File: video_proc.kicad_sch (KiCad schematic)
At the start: 0 parts

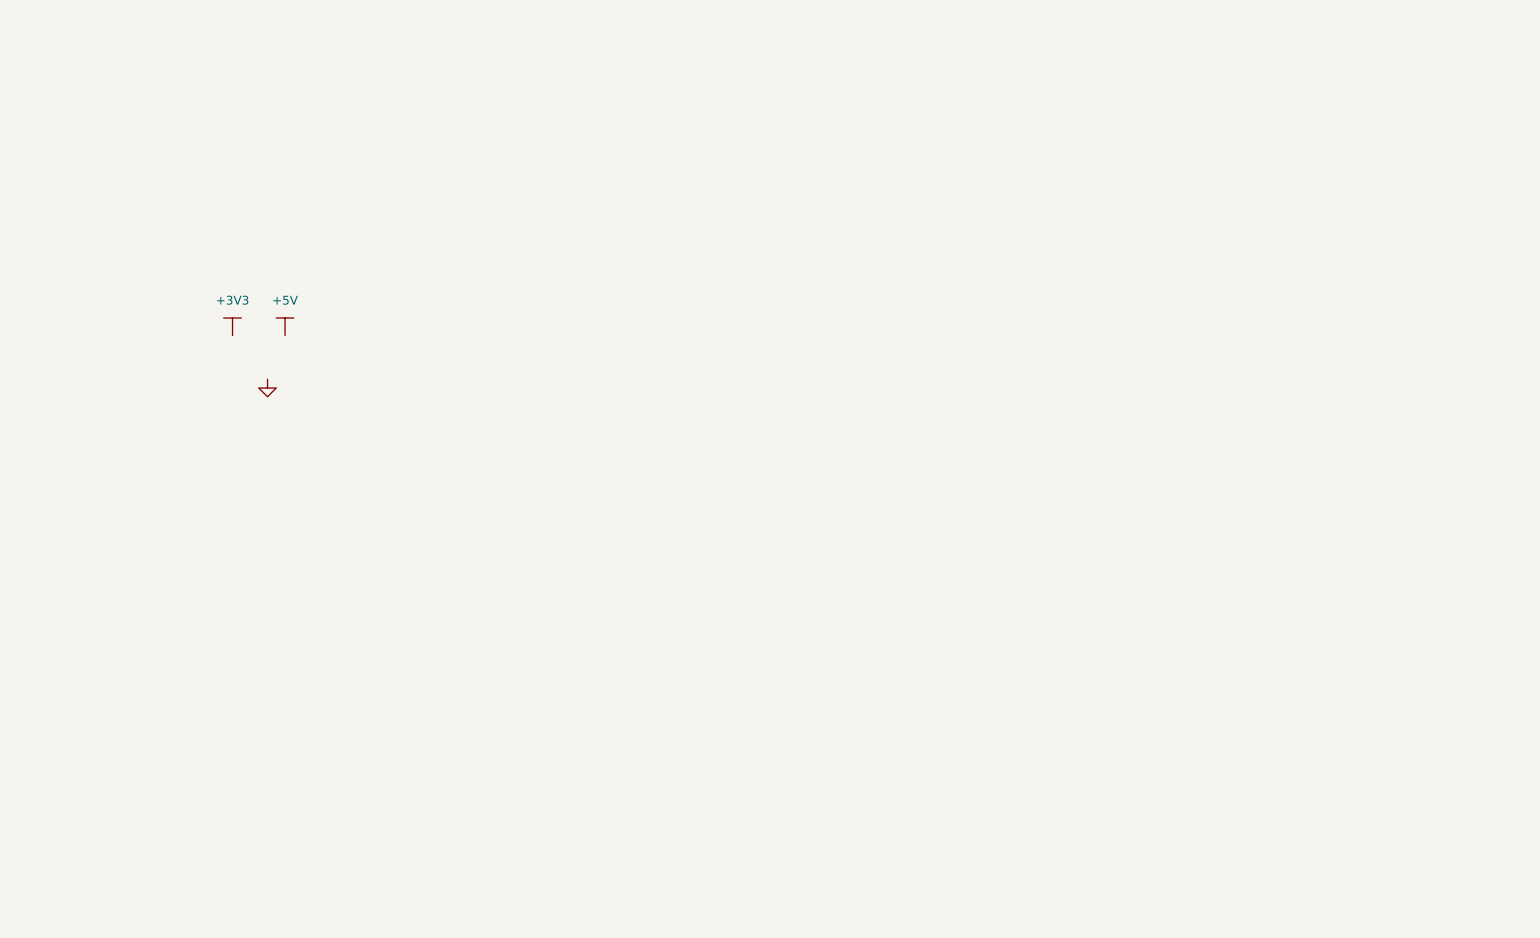
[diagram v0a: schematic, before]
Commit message: changed hierarchy, added symbols
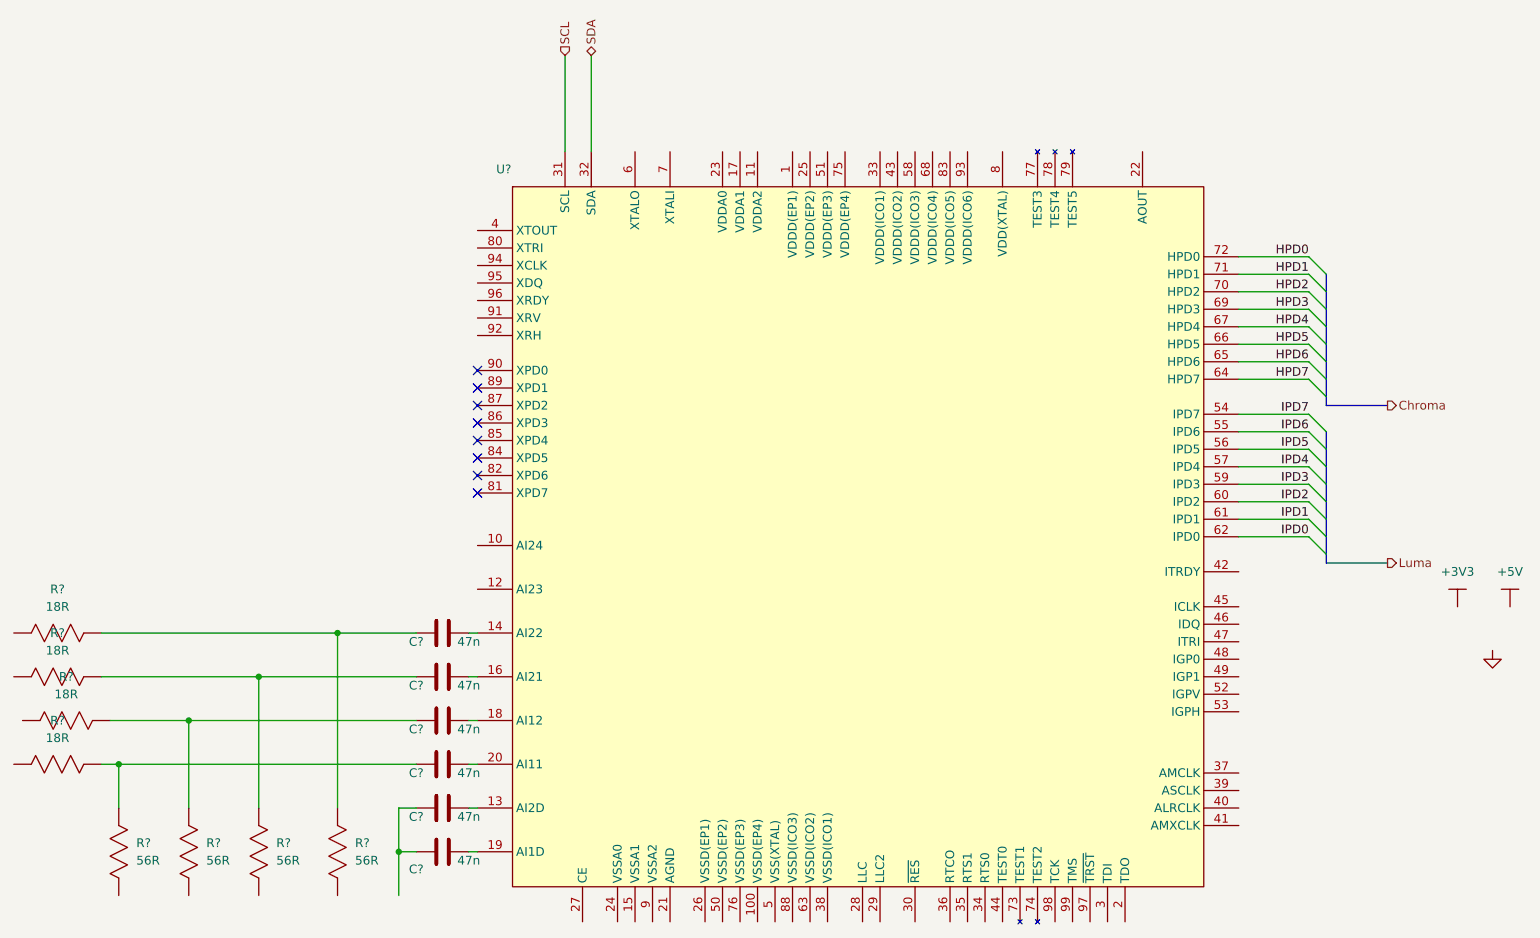
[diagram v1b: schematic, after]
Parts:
- added C? (x6): 47n, symbol tbc:GCJ188R71E473KA01D
- added R? (x4): 18R, symbol tbc:RC0603FR-0718RL
- added R? (x4): 56R, symbol tbc:RC0603FR-0756RL
- added U?: ~, symbol tbc:SAA7114H
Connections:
- new net: C?.1, R?.2, R?.2 (x4)
- new net: C?.2, U?.18 (AI12)
- new net: C?.2, U?.13 (AI2D)
- new net: C?.2, U?.14 (AI22)
- new net: C?.2, U?.16 (AI21)
- new net: C?.2, U?.19 (AI1D)
- new net: C?.2, U?.20 (AI11)
- new net: C?.1, C?.1
- new net HPD0: U?.72 (HPD0)
- new net HPD1: U?.71 (HPD1)
- new net HPD2: U?.70 (HPD2)
- new net HPD3: U?.69 (HPD3)
- new net HPD4: U?.67 (HPD4)
- new net HPD5: U?.66 (HPD5)
- new net HPD6: U?.65 (HPD6)
- new net HPD7: U?.64 (HPD7)
- new net IPD0: U?.62 (IPD0)
- new net IPD1: U?.61 (IPD1)
- new net IPD2: U?.60 (IPD2)
- new net IPD3: U?.59 (IPD3)
- new net IPD4: U?.57 (IPD4)
- new net IPD5: U?.56 (IPD5)
- new net IPD6: U?.55 (IPD6)
- new net IPD7: U?.54 (IPD7)
- new net SCL: U?.31 (SCL)
- new net SDA: U?.32 (SDA)
- no-connect marks 0 -> 8
